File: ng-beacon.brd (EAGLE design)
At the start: 71.1 x 76.2 mm, 7 parts

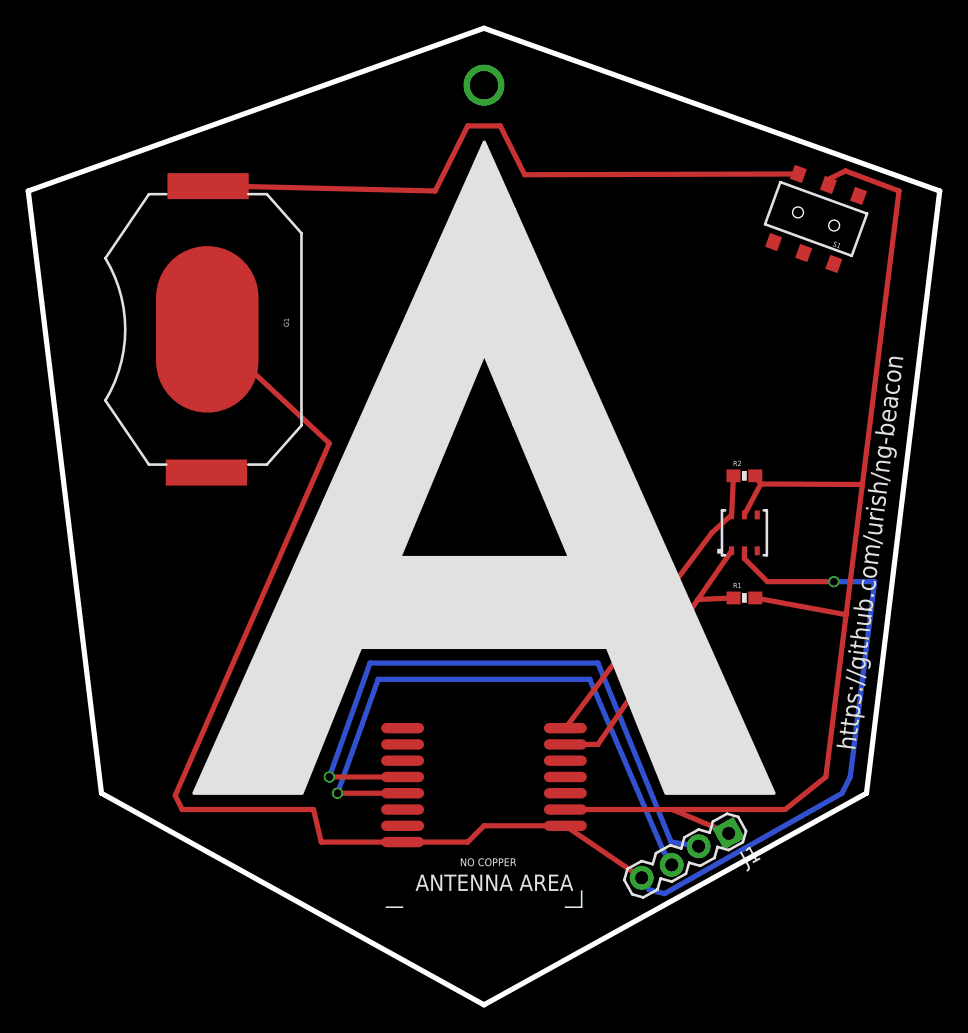
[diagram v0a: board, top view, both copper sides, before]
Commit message: improve routing, switch to SparkFun DRU
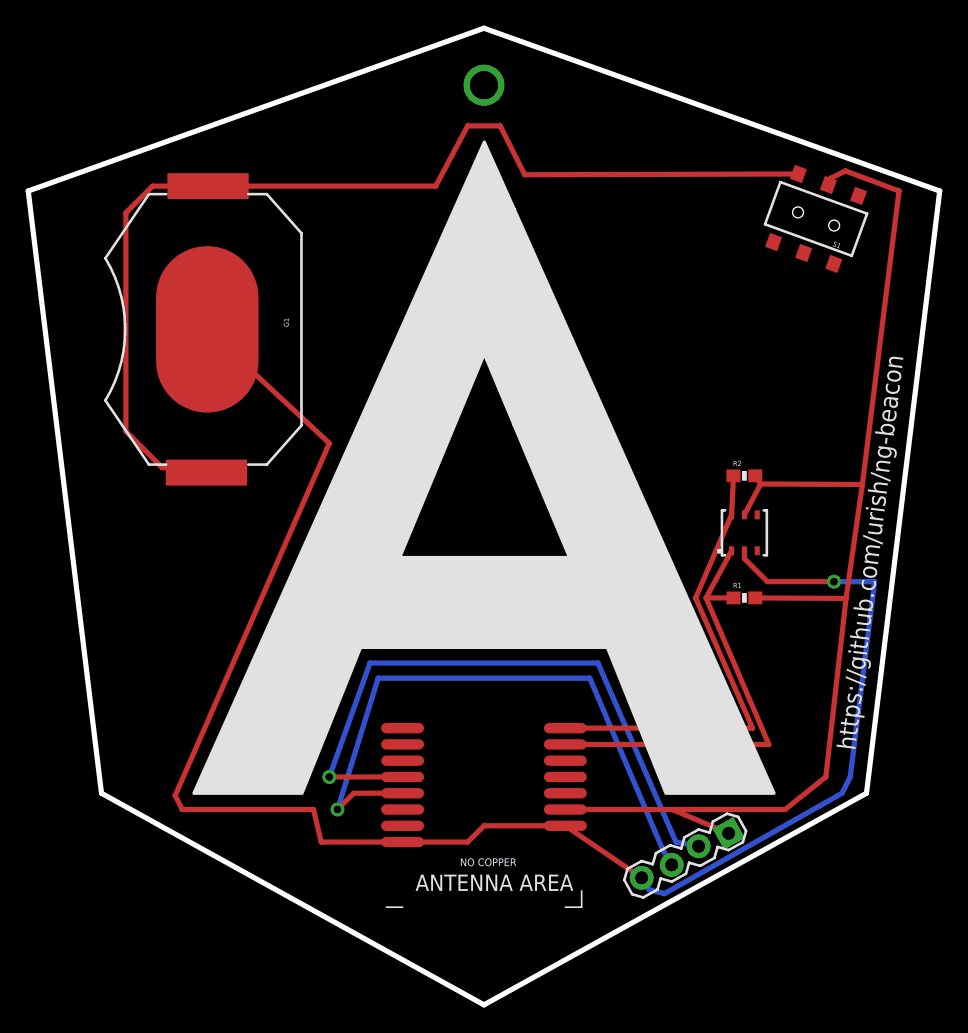
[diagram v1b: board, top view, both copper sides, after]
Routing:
- net N$1: track 50.0 -> 86.9 mm
- net SCL: track 24.2 -> 35.8 mm
- net SDA: track 23.7 -> 34.6 mm
- net SWCLK: track 46.9 -> 48.8 mm

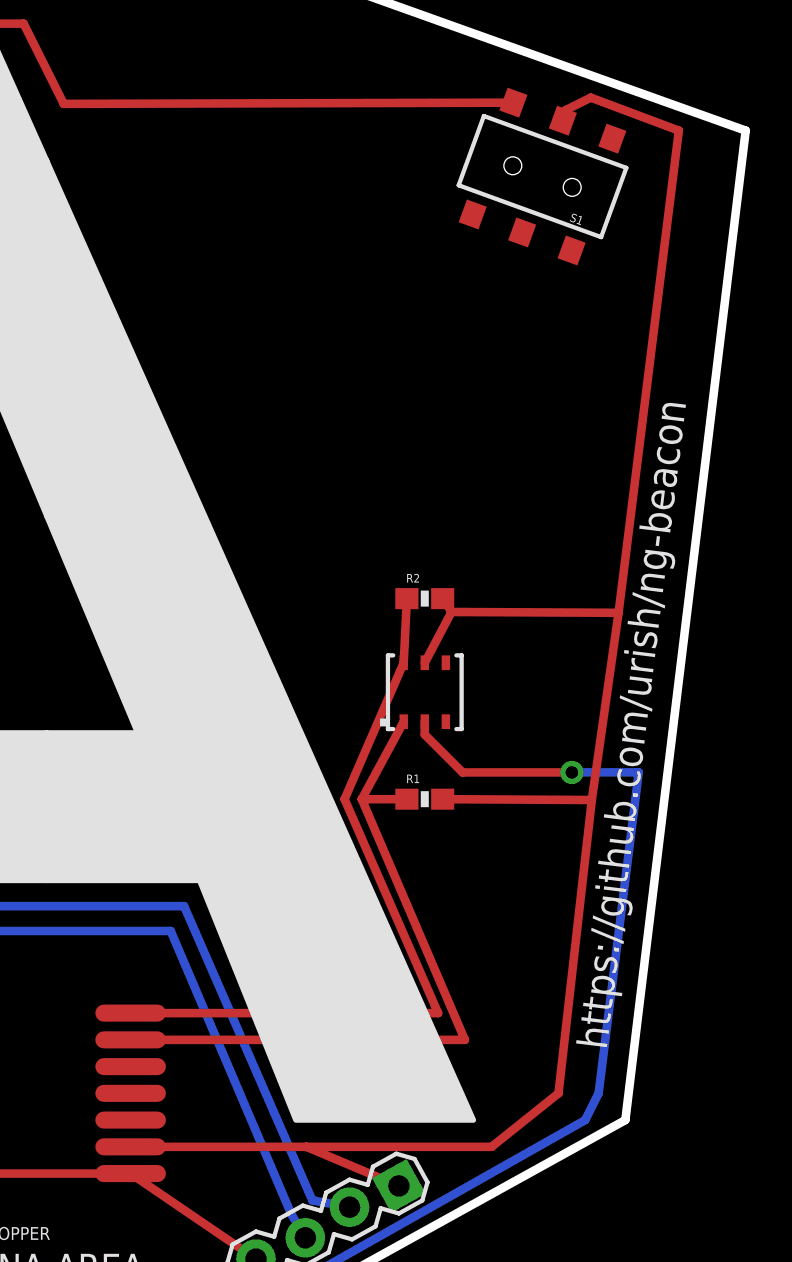
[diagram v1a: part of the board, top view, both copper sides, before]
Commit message: feat(pcb): initial effort adding an IMU
MPU-9250: includes accelerometer, gyroscope, compass
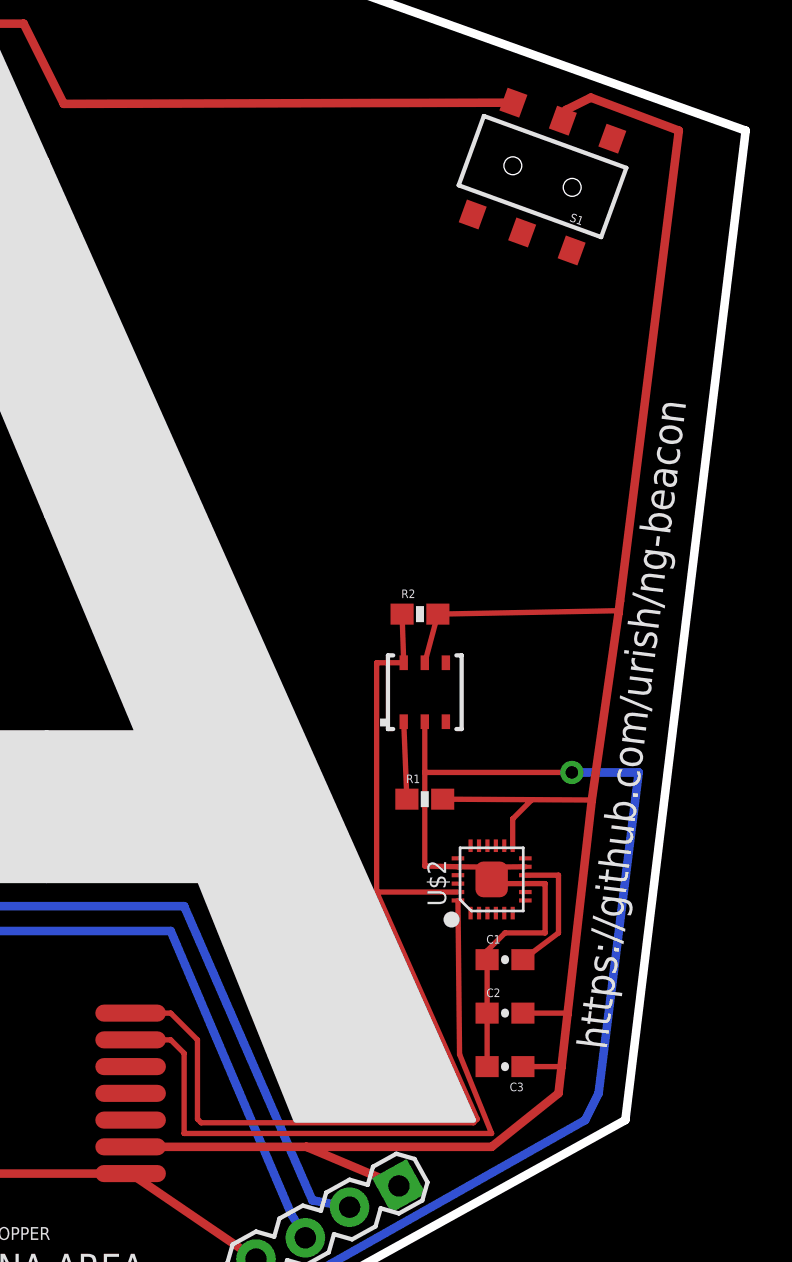
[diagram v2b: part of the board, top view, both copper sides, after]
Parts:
- added C1, C3: 0.1µF, SparkFun-Capacitors:0603-CAP
- added C2: 10nF, SparkFun-Capacitors:0603-CAP
- added U$2: MPU-9250, invensense:LEAD-QFN24
- moved R2 0.77 mm to (65.8, 39.3)
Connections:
- new net N$4: C1.2, U$2.10
- net GND: now also C1.1, C2.1, C3.2, U$2.11, U$2.18, U$2.20, U$2.25, U$2.9
- net SCL: now also U$2.23
- net SDA: now also U$2.24
- net VIN: now also C2.2, C3.1, U$2.1, U$2.13, U$2.22, U$2.8
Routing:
- net GND: track 130.4 -> 154.9 mm
- net SCL: track 35.8 -> 51.0 mm
- net N$4: track 0.00 -> 6.43 mm
- net VIN: track 96.9 -> 103.0 mm
- net SDA: track 34.6 -> 36.3 mm
